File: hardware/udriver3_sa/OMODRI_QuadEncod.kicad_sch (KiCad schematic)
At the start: 3 parts, among them U3 AS5047U

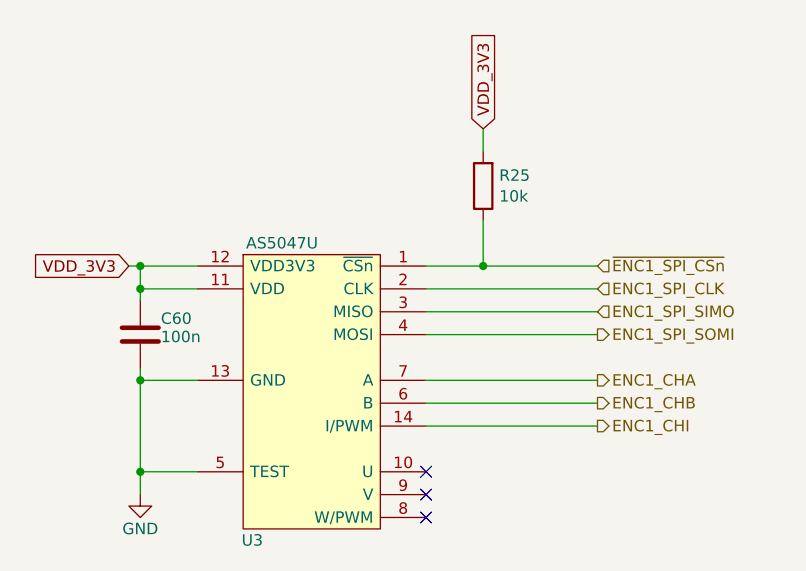
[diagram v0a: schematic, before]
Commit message: Update on uOmodri_SA. Remove USB, com SPI & debug connectors for integration into Myactuator motors. Connectors replaced by a ZIF connector.
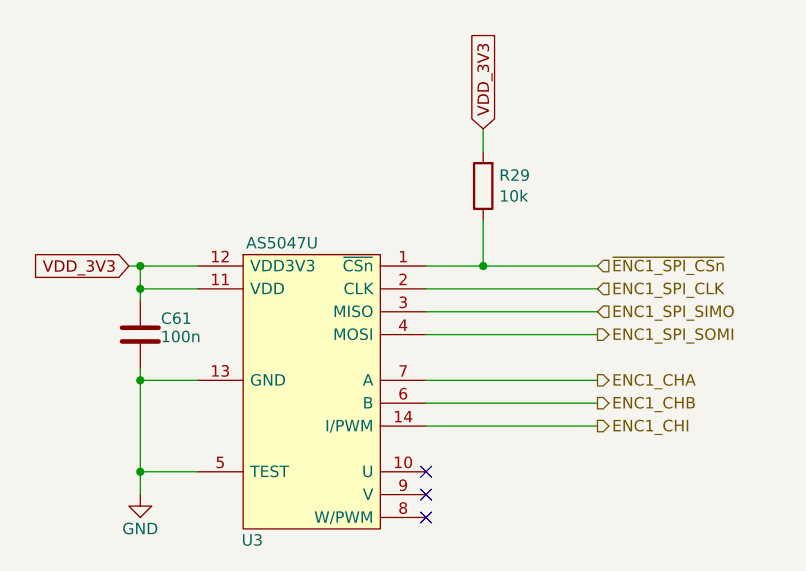
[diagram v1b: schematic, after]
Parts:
- renumbered C60 to C61, R25 to R29
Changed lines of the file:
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@@
 	(title_block
 		(title "Open MOtor DRiver Initiative  - Single Axis (OMODRI_SA)")
-		(date "2024-03-20")
+		(date "2024-11-08")
 		(rev "1.0")
 		(company "LAAS/CNRS")
@@
 		(on_board yes)
 		(dnp no)
-		(property "Reference" "#PWR080"
+		(property "Reference" "#PWR078"
 			(at 139.7 78.74 0)
 			(effects
@@
 			(project "omodri_sa_laas"
 				(path "/de5b13f0-933a-4c4d-9979-13dc57b13241/00000000-0000-0000-0000-00005f5a1016"
-					(reference "#PWR080")
+					(reference "#PWR078")
 					(unit 1)
 				)
@@
 		(on_board yes)
 		(dnp no)
-		(property "Reference" "C60"
+		(property "Reference" "C61"
 			(at 141.986 52.832 0)
 			(effects
@@
 			(project "omodri_sa_laas"
 				(path "/de5b13f0-933a-4c4d-9979-13dc57b13241/00000000-0000-0000-0000-00005f5a1016"
-					(reference "C60")
+					(reference "C61")
 					(unit 1)
 				)
@@
 		(on_board yes)
 		(dnp no)
-		(property "Reference" "R25"
+		(property "Reference" "R29"
 			(at 179.578 36.9316 0)
 			(effects
@@
 			(project "omodri_sa_laas"
 				(path "/de5b13f0-933a-4c4d-9979-13dc57b13241/00000000-0000-0000-0000-00005f5a1016"
-					(reference "R25")
+					(reference "R29")
 					(unit 1)
 				)
